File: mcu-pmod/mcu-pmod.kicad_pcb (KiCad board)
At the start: 4 copper layers, 41 x 31 mm, 51 parts, among them J1 PMOD_DEVICE, J2 XILINX_JTAG, J3 CONN_01X03, J4 CONN_01X03, J5 PMOD_HOST, U1 STM32H735-UFBGA176-25, U2 AT24MAC402

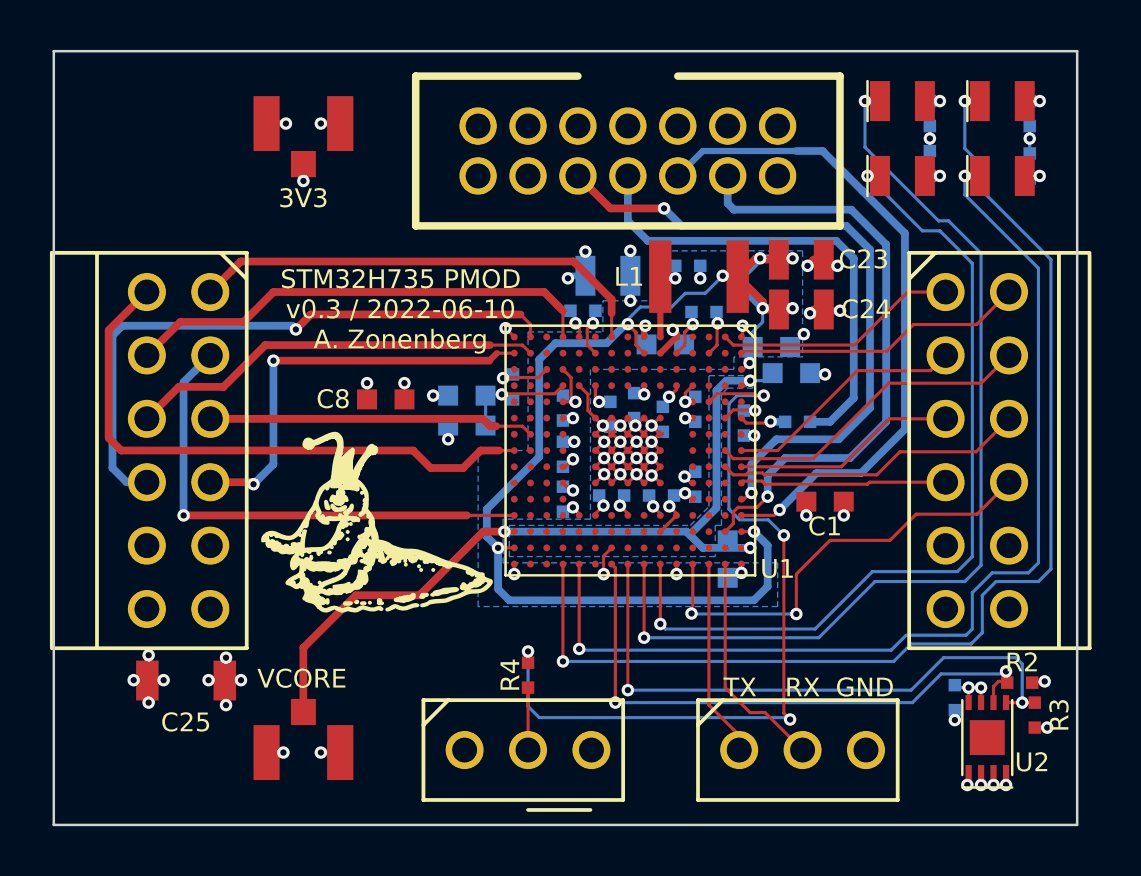
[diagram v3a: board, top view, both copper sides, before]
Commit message: Fixed TX/RX swap in schematic
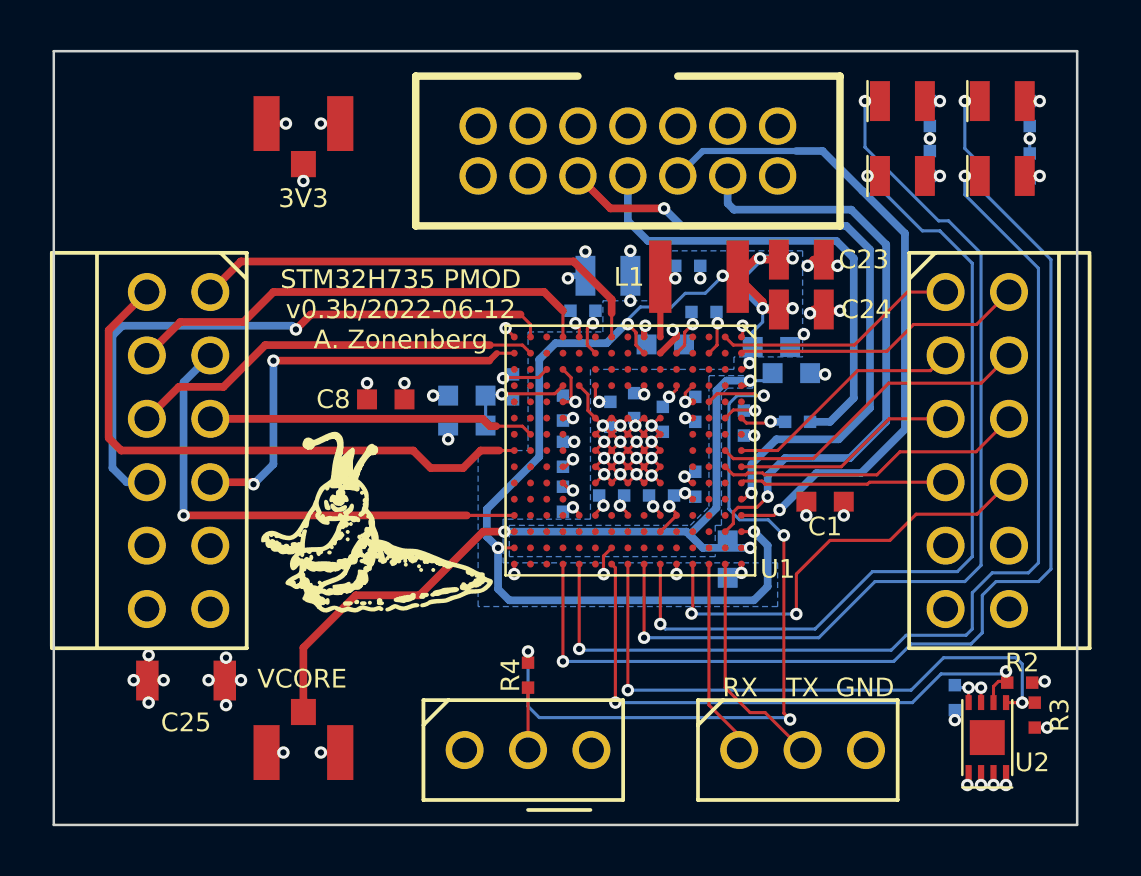
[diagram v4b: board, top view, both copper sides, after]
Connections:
- J3 pad 1: /UART_TX -> /UART_RX
- J3 pad 2: /UART_RX -> /UART_TX
- U1 pad B15: /UART_RX -> /UART_TX
- U1 pad C15: /UART_TX -> /UART_RX
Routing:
- net /UART_TX: track 7.95 -> 9.09 mm
- net /UART_RX: track 9.09 -> 7.95 mm
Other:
- board text added: "STM32H735 PMOD v0.3b/2022-06-12 A. Zonenberg"
- board text removed: "STM32H735 PMOD v0.3 / 2022-06-10 A. Zonenberg"
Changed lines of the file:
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@@
     (fp_line (start 3.81 -2) (end -4.19 -2) (layer "F.SilkS") (width 0.15))
     (pad "1" thru_hole circle (at -2.54 0) (size 1.524 1.524) (drill 1) (layers *.Cu *.Mask)
-      (net 30 "/UART_TX") (pinfunction "P1") (pintype "passive"))
+      (net 31 "/UART_RX") (pinfunction "P1") (pintype "passive"))
     (pad "2" thru_hole circle (at 0 0) (size 1.524 1.524) (drill 1) (layers *.Cu *.Mask)
-      (net 31 "/UART_RX") (pinfunction "P2") (pintype "passive"))
+      (net 30 "/UART_TX") (pinfunction "P2") (pintype "passive"))
     (pad "3" thru_hole circle (at 2.54 0) (size 1.524 1.524) (drill 1) (layers *.Cu *.Mask)
       (net 2 "/GND") (pinfunction "P3") (pintype "passive"))
@@
       (net 44 "unconnected-(U1-PadB14)") (pinfunction "PA8") (pintype "bidirectional+no_connect"))
     (pad "B15" smd circle (at 4.55 -3.9 270) (size 0.275 0.275) (layers "F.Cu" "F.Paste" "F.Mask")
-      (net 31 "/UART_RX") (pinfunction "UART4_TX") (pintype "output"))
+      (net 30 "/UART_TX") (pinfunction "UART4_TX") (pintype "output"))
     (pad "C1" smd circle (at -4.55 -3.25 270) (size 0.275 0.275) (layers "F.Cu" "F.Paste" "F.Mask")
       (net 144 "unconnected-(U1-PadC1)") (pinfunction "PC13") (pintype "bidirectional+no_connect"))
@@
       (net 55 "unconnected-(U1-PadC14)") (pinfunction "PA10") (pintype "bidirectional+no_connect"))
     (pad "C15" smd circle (at 4.55 -3.25 270) (size 0.275 0.275) (layers "F.Cu" "F.Paste" "F.Mask")
-      (net 30 "/UART_TX") (pinfunction "UART4_RX") (pintype "input"))
+      (net 31 "/UART_RX") (pinfunction "UART4_RX") (pintype "input"))
     (pad "D1" smd circle (at -4.55 -2.6 270) (size 0.275 0.275) (layers "F.Cu" "F.Paste" "F.Mask")
       (net 56 "unconnected-(U1-PadD1)") (pinfunction "PC15") (pintype "bidirectional+no_connect"))
@@
   (gr_line (start 87 45) (end 46 45) (layer "Edge.Cuts") (width 0.1))
   (gr_line (start 87 76) (end 87 45) (layer "Edge.Cuts") (width 0.1))
-  (gr_text "TX" (at 73.5 70.5) (layer "F.SilkS")
+  (gr_text "TX" (at 76 70.5) (layer "F.SilkS")
     (effects (font (size 0.75 0.75) (thickness 0.1)))
   )
-  (gr_text "RX" (at 76 70.5) (layer "F.SilkS")
+  (gr_text "RX" (at 73.5 70.5) (layer "F.SilkS")
     (effects (font (size 0.75 0.75) (thickness 0.1)))
   )
-  (gr_text "STM32H735 PMOD\nv0.3 / 2022-06-10\nA. Zonenberg" (at 59.9 55.35) (layer "F.SilkS")
+  (gr_text "STM32H735 PMOD\nv0.3b/2022-06-12\nA. Zonenberg" (at 59.9 55.35) (layer "F.SilkS")
     (effects (font (size 0.75 0.75) (thickness 0.1)))
   )
@@
   (segment (start 73.95 61.55) (end 74.95 60.55) (width 0.31) (layer "B.Cu") (net 26))
   (segment (start 71.15 52) (end 70.45 51.3) (width 0.31) (layer "B.Cu") (net 26))
-  (segment (start 72.25 65.55) (end 72.25 71.2) (width 0.125) (layer "F.Cu") (net 30))
-  (segment (start 73.46 72.41) (end 73.46 73) (width 0.125) (layer "F.Cu") (net 30))
-  (segment (start 72.25 71.2) (end 73.46 72.41) (width 0.125) (layer "F.Cu") (net 30))
-  (segment (start 72.9 70.5) (end 73.9 71.5) (width 0.125) (layer "F.Cu") (net 31))
-  (segment (start 72.9 65.55) (end 72.9 70.5) (width 0.125) (layer "F.Cu") (net 31))
-  (segment (start 74.5 71.5) (end 76 73) (width 0.125) (layer "F.Cu") (net 31))
-  (segment (start 73.9 71.5) (end 74.5 71.5) (width 0.125) (layer "F.Cu") (net 31))
+  (segment (start 72.9 70.5) (end 73.9 71.5) (width 0.125) (layer "F.Cu") (net 30))
+  (segment (start 72.9 65.55) (end 72.9 70.5) (width 0.125) (layer "F.Cu") (net 30))
+  (segment (start 74.5 71.5) (end 76 73) (width 0.125) (layer "F.Cu") (net 30))
+  (segment (start 73.9 71.5) (end 74.5 71.5) (width 0.125) (layer "F.Cu") (net 30))
+  (segment (start 72.25 65.55) (end 72.25 71.2) (width 0.125) (layer "F.Cu") (net 31))
+  (segment (start 73.46 72.41) (end 73.46 73) (width 0.125) (layer "F.Cu") (net 31))
+  (segment (start 72.25 71.2) (end 73.46 72.41) (width 0.125) (layer "F.Cu") (net 31))
   (segment (start 65 73) (end 65 70.5) (width 0.125) (layer "F.Cu") (net 32))
   (segment (start 73.55 59.7) (end 73.75 59.9) (width 0.125) (layer "F.Cu") (net 33))
